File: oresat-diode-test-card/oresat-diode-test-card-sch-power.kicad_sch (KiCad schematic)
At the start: 89 parts, among them Q1 DMP2240UDM, Q2 DMP3050LVT-7, Q7 MOSFET-PCH-SOT23-6, Q8 PMV45EN, Q9 PMV45EN, U10 TPS62111RSA, U11 MIC842LYC5, U12 MIC842LYC5, U2 MAX7310, U3 TS5A21366DCUR, U6 MAX4211

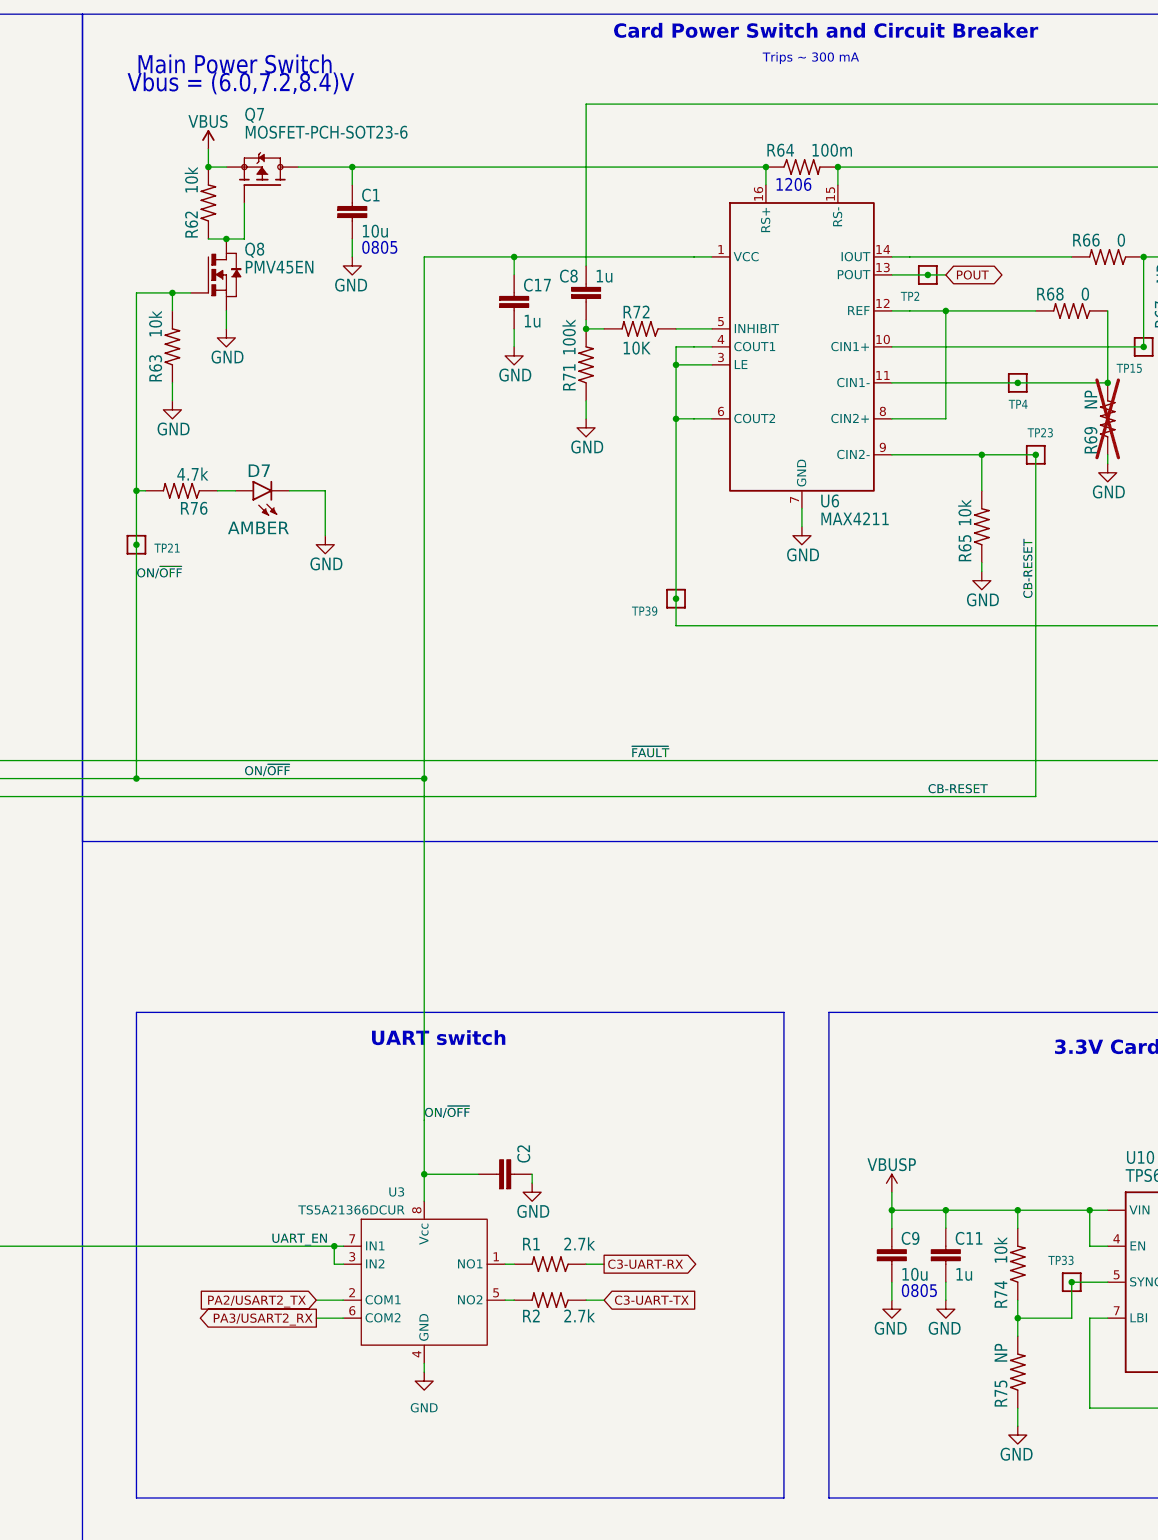
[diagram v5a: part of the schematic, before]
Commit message: BOM changes! Now up to date.
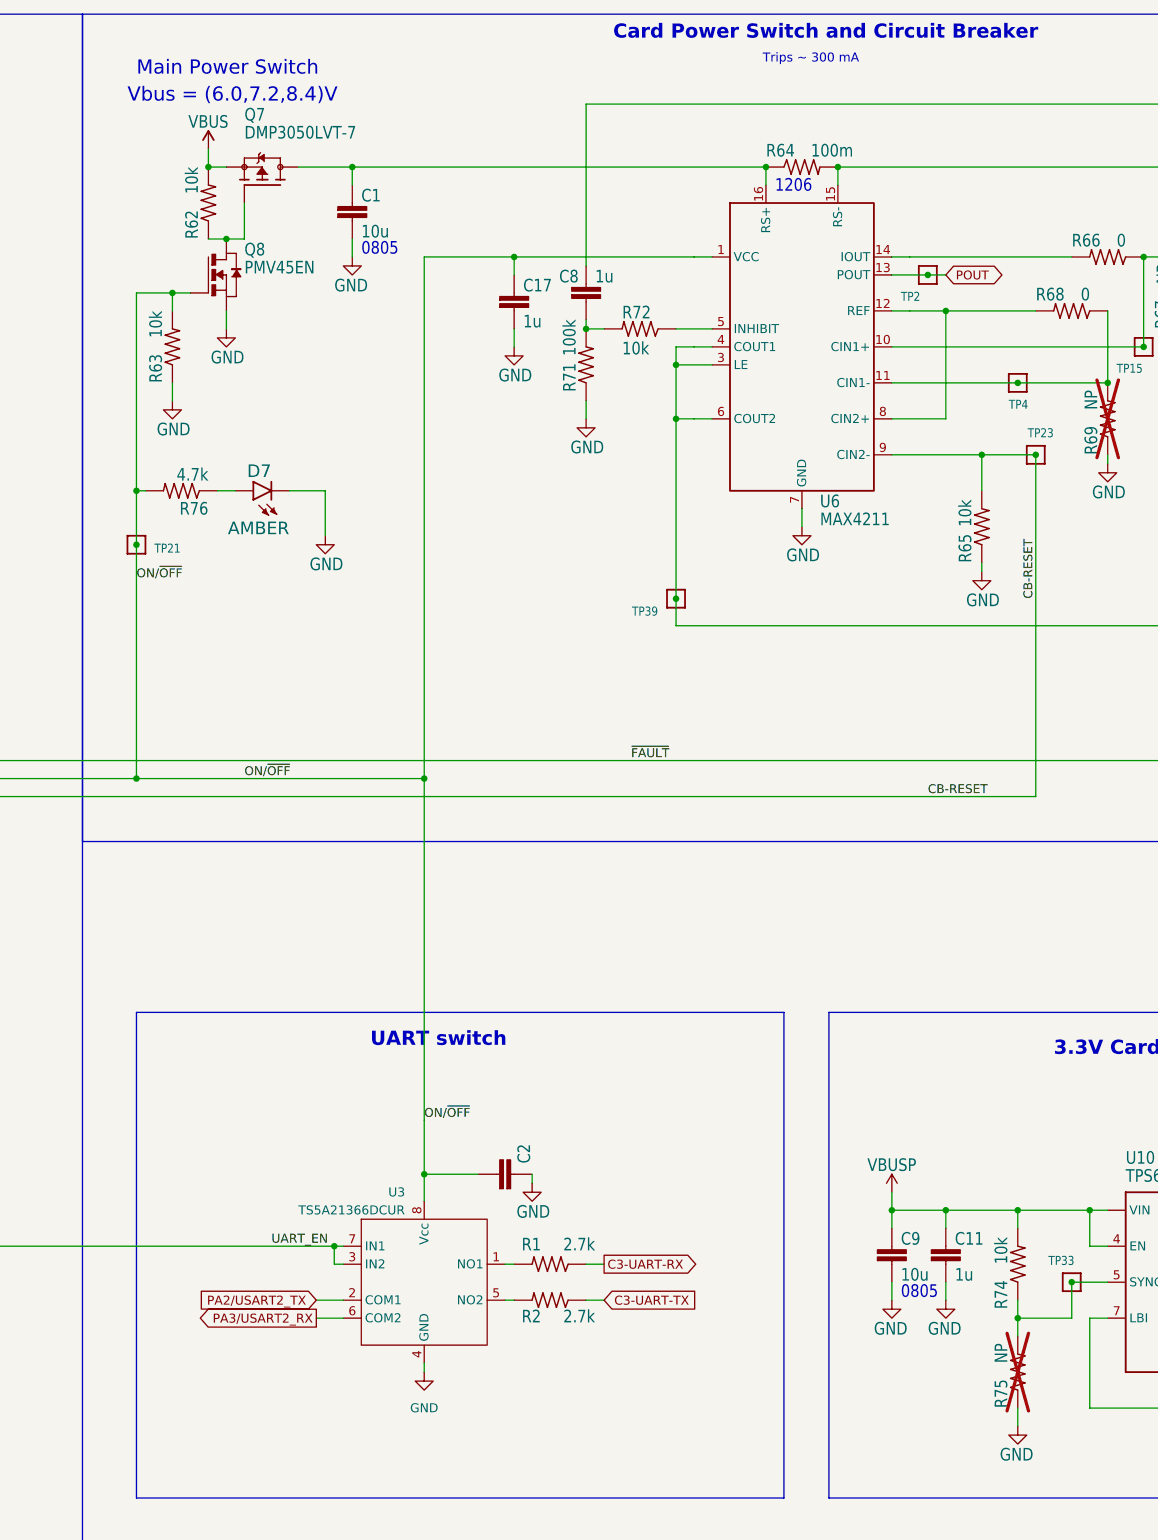
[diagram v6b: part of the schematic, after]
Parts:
- C1, C9: DIS Digi-Key -> (none); DPN 1276-6472-1-ND -> 490-GRT21BC71E106KE13LCT-ND; DST Digi-Key -> DigiKey; MFR Samsung -> Murata Electronics; MPN CL21B106KOQNNNG -> GRT21BC71E106KE13L
- C11, C17, C22, C23: DIS Digi-Key -> (none); DPN 311-1444-1-ND -> 587-3473-1-ND; DST Digi-Key -> DigiKey; MFR Yageo -> Taiyo Yuden; MPN CC0603KRX5R7BB105 -> TMK107BJ105KAHT
- C16: DIS Digi-Key -> (none); DST Digi-Key -> DigiKey; MFR Murata -> Murata Electronics
- C2: value CL10B104KB8NNNL -> 100n; DPN (none) -> 587-3472-1-ND; DST (none) -> DigiKey; MFR (none) -> Taiyo Yuden; MPN (none) -> TMK107BJ104KAHT
- C3: DIS Digi-Key -> (none); DPN 399-14941-1-ND -> 587-3472-1-ND; DST Digi-Key -> DigiKey; MFR Kemet -> Taiyo Yuden; MPN C0603C104K4PAC7867 -> TMK107BJ104KAHT
- C4: DPN (none) -> 587-3476-1-ND; DST (none) -> DigiKey; MFR (none) -> Taiyo Yuden; MPN (none) -> TMK107BJ474KAHT
- C5: DPN (none) -> 399-14102-1-ND; DST (none) -> DigiKey; MFR (none) -> KEMET; MPN (none) -> C0603C103J3GECAUTO
- C8: DPN (none) -> 587-3473-1-ND; DST (none) -> DigiKey; MFR (none) -> Taiyo Yuden; MPN (none) -> TMK107BJ105KAHT
- D3, D6: DIS Digi-Key -> (none); DPN 511-1584-1-ND -> 732-4971-1-ND; DST Digi-Key -> DigiKey; MFR Rohm -> Wurth; MPN SML-E12M8WT86 -> 150060GS75000
- D7: DIS Digi-Key -> (none); DPN 1830-1064-1-ND -> 732-150060AS75000CT-ND; DST Digi-Key -> DigiKey; MFR Inolux -> Wurth; MPN IN-S63AT5A -> 150060AS75000
- L1, Q1, R39, R40, R45, R52, R53, R55, R56, R57, R59, R67, R69, U10: DIS Digi-Key -> (none); DST Digi-Key -> DigiKey
- Q2: footprint oresat-proto-card:SOT23-6 -> Package_TO_SOT_SMD:SOT-23-6; DIS Digi-Key -> (none); DST Digi-Key -> DigiKey
- Q7: value MOSFET-PCH-SOT23-6 -> DMP3050LVT-7; footprint oresat-proto-card:SOT23-6 -> Package_TO_SOT_SMD:SOT-23-6; DIS Digi-Key -> (none); DST Digi-Key -> DigiKey
- Q8, Q9: footprint oresat-proto-card:SOT23 -> Package_TO_SOT_SMD:SOT-23-3; DIS Digi-Key -> (none); DST Digi-Key -> DigiKey
- R1, R2: DPN (none) -> RMCF0603FT2K70CT-ND; DST (none) -> DigiKey; MFR (none) -> Stackpole Electronics Inc; MPN (none) -> RMCF0603FT2K70
- R17: DIS Digi-Key -> (none); DPN P2.7KDBCT-ND -> RMCF0603FT2K70CT-ND; DST Digi-Key -> DigiKey; MFR Panasonic -> Stackpole Electronics Inc; MPN ERA-3AEB272V -> RMCF0603FT2K70
- R24: DIS Digi-Key -> (none); DPN 311-10.0HRCT-ND -> RMCF0603FT10R0CT-ND; DST Digi-Key -> DigiKey; MFR Yageo -> Stackpole Electronics Inc; MPN RC0603FR-0710RL -> RMCF0603FT10R0
- R3: DIS Digi-Key -> (none); DPN P2.7KDBCT-ND -> RMCF0603FT10K0CT-ND; DST Digi-Key -> DigiKey; MFR Panasonic -> Stackpole Electronics Inc; MPN ERA-3AEB272V -> RMCF0603FT10K0
- R4, R5: value RC0603FR-0710KL -> 10k; DPN (none) -> RMCF0603FT10K0CT-ND; DST (none) -> DigiKey; MFR (none) -> Stackpole Electronics Inc; MPN (none) -> RMCF0603FT10K0
- R46, R54, R58: DIS Digi-Key -> (none); DPN 1276-4275-1-ND -> RMCF0603FT2K70CT-ND; DST Digi-Key -> DigiKey; MFR Samsung -> Stackpole Electronics Inc; MPN RC1005F6653CS -> RMCF0603FT2K70
- R60, R80: DIS Digi-Key -> (none); DPN 311-100HRCT-ND -> RMCF0603FT100RCT-ND; DST Digi-Key -> DigiKey; MFR Yageo -> Stackpole Electronics Inc; MPN RC0603FR-07100RL -> RMCF0603FT100R
- R61, R62, R63, R65, R70, R73, R74: DIS Digi-Key -> (none); DPN RNCP0603FTD10K0CT-ND -> RMCF0603FT10K0CT-ND; DST Digi-Key -> DigiKey; MFR Stackpole -> Stackpole Electronics Inc; MPN RNCP0603FTD10K0 -> RMCF0603FT10K0
- R64: DIS Digi-Key -> (none); DPN CSR1206FTR100CT-ND -> 846-UCR18EVHFLR100CT-ND; DST Digi-Key -> DigiKey; MFR Stackpole -> Rohm Semiconductor; MPN CSR1206FTR100 -> UCR18EVHFLR100
- R66, R68: DIS Digi-Key -> (none); DPN 311-0.0GRCT-ND -> RMCF0603ZT0R00CT-ND; DST Digi-Key -> DigiKey; MFR Yageo -> Stackpole Electronics Inc; MPN RC0603JR-070RL -> RMCF0603ZT0R00
- R71: DIS Digi-Key -> (none); DPN 1276-4275-1-ND -> RMCF0603FT100KCT-ND; DST Digi-Key -> DigiKey; MFR Samsung -> Stackpole Electronics Inc; MPN RC1005F6653CS -> RMCF0603FT100K
- R72: value 10K -> 10k; DIS Digi-Key -> (none); DPN 1276-4275-1-ND -> RMCF0603FT10K0CT-ND; DST Digi-Key -> DigiKey; MFR Samsung -> Stackpole Electronics Inc; MPN RC1005F6653CS -> RMCF0603FT10K0
- R75: DIS Digi-Key -> (none); DST Digi-Key -> DigiKey; now not fitted; now left out of the parts list
- R76: DIS Digi-Key -> (none); DPN P2.7KDBCT-ND -> RMCF0603FT4K70CT-ND; DST Digi-Key -> DigiKey; MFR Panasonic -> Stackpole Electronics Inc; MPN ERA-3AEB272V -> RMCF0603FT4K70
- R77, R81: DIS Digi-Key -> (none); DPN RNCP0603FTD10K0CT-ND -> RMCF0603FT665KCT-ND; DST Digi-Key -> DigiKey; MFR Stackpole -> Stackpole Electronics Inc; MPN RNCP0603FTD10K0 -> RMCF0603FT665K
- R78, R82: DIS Digi-Key -> (none); DPN A129718CT-ND -> RMCF0603FT330KCT-ND; DST Digi-Key -> DigiKey; MFR TE Connectivity -> Stackpole Electronics Inc; MPN CRGCQ0603F330K -> RMCF0603FT330K
- R79, R83: DIS Digi-Key -> (none); DPN 311-1.00MHRCT-ND -> RMCF0603FT1M00CT-ND; DST Digi-Key -> DigiKey; MFR Yageo -> Stackpole Electronics Inc; MPN RC0603FR-071ML -> RMCF0603FT1M00
- TP15, TP2, TP21, TP23, TP24, TP301, TP31, TP32, TP33, TP34, TP35, TP36, TP37, TP38, TP39, TP4, TP40, TP41, TP42: DPN (none) -> N/A; DST (none) -> N/A; MFR (none) -> N/A; MPN (none) -> N/A; now left out of the parts list
- U11, U12: DPN (none) -> 576-2927-1-ND; DST (none) -> DigiKey; MFR (none) -> Microchip; MPN (none) -> MIC842LYC5-TR
- U2: DIS Digi-Key -> (none); DST Digi-Key -> DigiKey; MFR Maxim -> Analog Devices Inc./Maxim Integrated; MPN MAX7310ATE -> MAX7310ATE+
- U3: DST Digi-Key -> DigiKey
- U6: DIS Digi-Key -> (none); DST Digi-Key -> DigiKey; MFR Maxim -> Analog Devices Inc./Maxim Integrated
